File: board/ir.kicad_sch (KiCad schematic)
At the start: 7 parts, among them Q4 DMG2302U

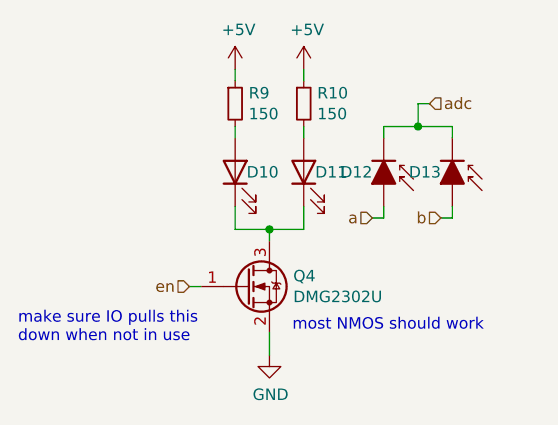
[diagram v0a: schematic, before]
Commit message: adapt to BAC standard capability
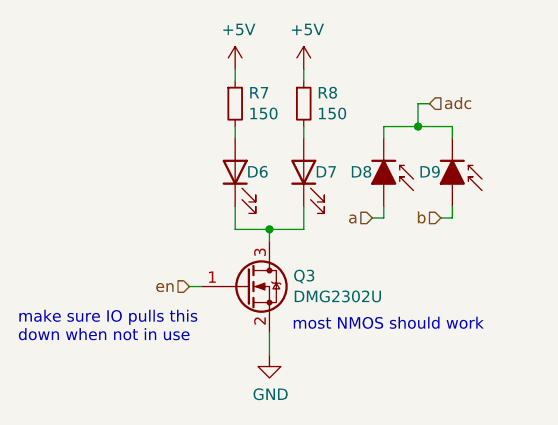
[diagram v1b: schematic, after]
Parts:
- D8: renamed from D12; symbol Device:D_Photo_ALT -> Device:D_Photo_Filled
- D9: renamed from D13; symbol Device:D_Photo_ALT -> Device:D_Photo_Filled
- renumbered D10 to D6, D11 to D7, Q4 to Q3, R9 to R7, R10 to R8
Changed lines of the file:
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@@
     (effects (font (size 1.27 1.27)) (justify left))
   )
-  (symbol (lib_id "Device:D_Photo_ALT") (at 161.29 101.6 270)
+  (symbol (lib_id "Device:D_Photo_Filled") (at 161.29 101.6 270)
     (in_bom yes) (on_board yes)
-    (property "Reference" "D13" (id 0) (at 160.02 100.33 90)
+    (property "Reference" "D9" (id 0) (at 160.02 100.33 90)
       (effects (font (size 1.27 1.27)) (justify right))
     )
@@
     (pin "2")
   )
-  (symbol (lib_id "Device:D_Photo_ALT") (at 153.67 101.6 270)
+  (symbol (lib_id "Device:D_Photo_Filled") (at 153.67 101.6 270)
     (in_bom yes) (on_board yes)
-    (property "Reference" "D12" (id 0) (at 152.4 100.33 90)
+    (property "Reference" "D8" (id 0) (at 152.4 100.33 90)
       (effects (font (size 1.27 1.27)) (justify right))
     )
@@
   (symbol (lib_id "Device:LED") (at 137.16 100.33 90)
     (in_bom yes) (on_board yes)
-    (property "Reference" "D10" (id 0) (at 138.43 100.33 90)
+    (property "Reference" "D6" (id 0) (at 138.43 100.33 90)
       (effects (font (size 1.27 1.27)) (justify right))
     )
@@
   (symbol (lib_id "Device:LED") (at 144.78 100.33 90)
     (in_bom yes) (on_board yes)
-    (property "Reference" "D11" (id 0) (at 146.05 100.33 90)
+    (property "Reference" "D7" (id 0) (at 146.05 100.33 90)
       (effects (font (size 1.27 1.27)) (justify right))
     )
@@
   (symbol (lib_id "Device:R_Small") (at 137.16 92.71 0)
     (in_bom yes) (on_board yes)
-    (property "Reference" "R9" (id 0) (at 138.6586 91.5416 0)
+    (property "Reference" "R7" (id 0) (at 138.6586 91.5416 0)
       (effects (font (size 1.27 1.27)) (justify left))
     )
@@
   (symbol (lib_id "Device:R_Small") (at 144.78 92.71 0)
     (in_bom yes) (on_board yes)
-    (property "Reference" "R10" (id 0) (at 146.2786 91.5416 0)
+    (property "Reference" "R8" (id 0) (at 146.2786 91.5416 0)
       (effects (font (size 1.27 1.27)) (justify left))
     )
@@
   (symbol (lib_id "Transistor_FET:DMG2302U") (at 138.43 113.03 0)
     (in_bom yes) (on_board yes)
-    (property "Reference" "Q4" (id 0) (at 143.6116 111.8616 0)
+    (property "Reference" "Q3" (id 0) (at 143.6116 111.8616 0)
       (effects (font (size 1.27 1.27)) (justify left))
     )
